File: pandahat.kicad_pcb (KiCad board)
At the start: 2 copper layers, 92 x 56 mm, 107 parts, among them CN1 Wago connector, CN2 Wago connector, CN3 Wago connector, CN4 Wago connector, CN5 Wago connector, CN6 Wago connector, CN7 Wago connector, J1 GPIO, J19 Conn_01x03, J2 Conn_02x03_Odd_Even, J20 Conn_01x03, J21 Conn_01x03, J3 Conn_01x04, SW1 TS-1187A-B-A-B, U1 AMS1117-3.3, U2 LM2596-5.0FW05ARHQ, U3 STM32F103C8T6, U6 LIS2DH12TR

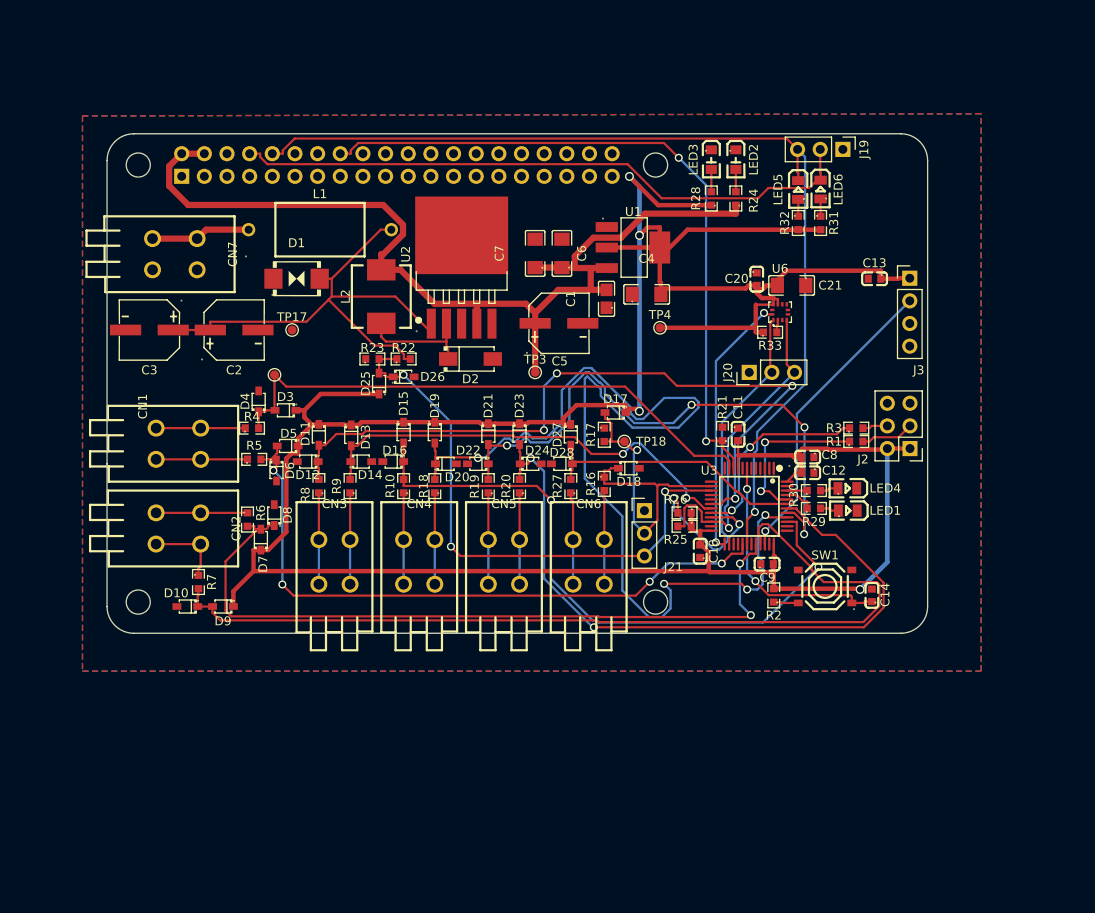
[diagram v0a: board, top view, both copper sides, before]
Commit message: changed IMU, reworked PCB layout
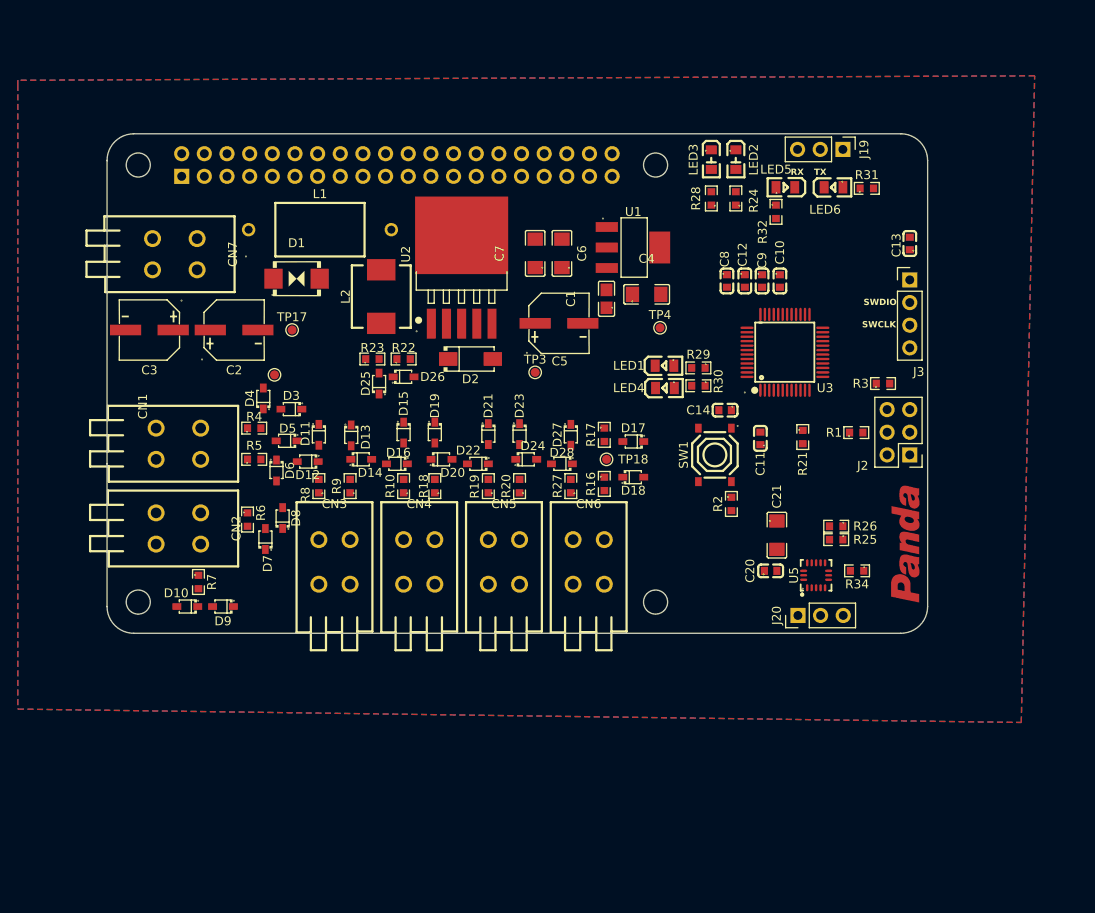
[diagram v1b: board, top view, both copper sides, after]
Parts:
- removed J21: Conn_01x03, Connector_PinHeader_2.54mm:PinHeader_1x03_P2.54mm_Vertical
- removed R33: 0603WAF1003T5E, easyeda2kicad:R0603
- removed U6: LIS2DH12TR, easyeda2kicad:LGA-12_L2.0-W2.0-P0.50-BL
- added G***: LOGO, LOGO, F.Cu at (189.5, 90.0)
- added R34: 0603WAF1003T5E, easyeda2kicad:R0603, F.Cu at (184.1, 93.0)
- added U5: LIS3DHTR_C15134, easyeda2kicad:LGA-16_L3.0-W3.0-P0.50-TL, F.Cu at (179.5, 93.5)
- moved C20 32.7 mm to (174.4, 93.0), turned to 0 degrees
- moved C9 31.8 mm to (173.4, 60.5), turned to -90 degrees
- moved C10 31.6 mm to (175.4, 60.5), turned to -90 degrees
- moved C21 28.0 mm to (175.1, 89.0), turned to -90 degrees
- moved J20 27.8 mm to (177.5, 98.0)
- moved C14 26.5 mm to (169.3, 75.0), turned to 180 degrees
- moved LED1 26.2 mm to (162.5, 70.0), turned to 0 degrees
- moved LED4 23.3 mm to (162.6, 72.5), turned to 0 degrees
- moved C12 22.6 mm to (171.5, 60.5), turned to -90 degrees
- moved C8 21.7 mm to (169.5, 60.5), turned to -90 degrees
- moved R29 20.4 mm to (166.3, 70.2), turned to 180 degrees
- moved SW1 19.2 mm to (168.2, 80.0), turned to -90 degrees
- moved U3 17.7 mm to (176.0, 68.5), turned to 0 degrees
- moved R30 17.5 mm to (166.3, 72.2), turned to 180 degrees
- moved R25 17.1 mm to (181.8, 89.5)
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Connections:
- J3 pad 3: /MCU_IO/STM32/SWDCLK -> /MCU_IO/STM32/SWCLK
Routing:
- net +3.3V: track 329.9 -> 0.00 mm, vias 4 -> 0
- net /MCU_IO/INPUT7: track 119.9 -> 0.00 mm, vias 4 -> 0
- net /UART_RX: track 111.2 -> 0.00 mm, vias 1 -> 0
- net +5V: track 110.9 -> 0.00 mm
- net /MCU_IO/INPUT3: track 101.3 -> 0.00 mm
- net /MCU_IO/INPUT2: track 83.1 -> 0.00 mm, vias 2 -> 0
- net /MCU_IO/INPUT4: track 82.0 -> 0.00 mm, vias 4 -> 0
- net /MCU_IO/INPUT9: track 78.1 -> 0.00 mm, vias 2 -> 0
- net /GPIO23: track 77.9 -> 0.00 mm, vias 2 -> 0
- net /MCU_IO/INPUT1: track 73.3 -> 0.00 mm, vias 4 -> 0
- net /MCU_IO/INPUT6: track 72.6 -> 0.00 mm, vias 2 -> 0
- net /UART_TX: track 70.8 -> 0.00 mm
- net /MCU_IO/INPUT8: track 65.7 -> 0.00 mm, vias 4 -> 0
- net /MCU_IO/ANALOG1: track 63.9 -> 0.00 mm, vias 3 -> 0
- net /MCU_IO/INPUT0: track 63.5 -> 0.00 mm
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- added copper zone on In1.Cu, net GND
- added copper zone on In2.Cu, net GND
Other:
- copper layers 2 -> 4
- board text added: "RX"
- board text added: "SWCLK"
- board text added: "SWDIO"
- board text added: "TX"

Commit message: manual routing progress
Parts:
- moved C11 17.2 mm to (181.2, 62.8), turned to 180 degrees
- moved C8 16.7 mm to (177.2, 75.2), turned to 90 degrees
- moved R34 14.8 mm to (180.2, 78.8), turned to -90 degrees
- moved C20 14.3 mm to (173.2, 78.8), turned to -90 degrees
- moved L2 13.9 mm to (141.8, 70.8), turned to 0 degrees
- moved U5 13.7 mm to (177.2, 80.0)
- moved C6 13.4 mm to (149.5, 70.8), turned to 0 degrees
- moved C14 12.0 mm to (168.9, 87.0)
- moved SW1 12.0 mm to (167.8, 92.0)
- moved C12 11.2 mm to (168.2, 71.2), turned to 0 degrees
- moved C3 11.2 mm to (115.8, 68.0)
- moved TP3 10.6 mm to (153.2, 61.5)
- moved C7 10.4 mm to (149.5, 67.8), turned to 0 degrees
- moved R2 9.71 mm to (172.0, 95.0), turned to 0 degrees
- moved TP4 9.34 mm to (164.5, 56.8)
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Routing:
- net +3.3V: track 0.00 -> 222.2 mm
- net +5V: track 0.00 -> 115.1 mm, vias 0 -> 5
- net VPP: track 0.00 -> 35.8 mm
- net /MCU_IO/STM32/RESET: track 0.00 -> 19.7 mm, vias 0 -> 2
- net /MCU_IO/PB11_SDA: track 0.00 -> 19.4 mm, vias 0 -> 1
- net /MCU_IO/STM32/BOOT0: track 0.00 -> 19.1 mm, vias 0 -> 2
- net /MCU_IO/PB10_SCL: track 0.00 -> 17.7 mm, vias 0 -> 1
- net +BATT: track 0.00 -> 11.2 mm
- net /MCU_IO/Analog Input/ANALOG_IN: track 0.00 -> 10.5 mm
- net /MCU_IO/INPUT9/INPUT: track 0.00 -> 10.2 mm
- net /MCU_IO/INPUT8/INPUT: track 0.00 -> 10.2 mm
- net /MCU_IO/INPUT7/INPUT: track 0.00 -> 10.2 mm
- net /MCU_IO/INPUT6/INPUT: track 0.00 -> 10.2 mm
- net /MCU_IO/INPUT5/INPUT: track 0.00 -> 10.2 mm
- net /MCU_IO/INPUT4/INPUT: track 0.00 -> 10.2 mm
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- added copper zone on F.Cu, net +3.3V
- removed copper zone on In1.Cu, net GND
- removed copper zone on In2.Cu, net GND
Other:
- copper layers 4 -> 2

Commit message: more work
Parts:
- added D29: SS54_C22452, easyeda2kicad:SMA_L4.4-W2.8-LS5.4-R-RD, F.Cu at (119.7, 66.3)
- L2: value FXL0630-6R8-M -> 47uH; footprint easyeda2kicad:IND-SMD_L7.0-W6.6 -> easyeda2kicad:IND-SMD_L7.2-W6.6_GPSR07X0
- moved TP17 40.9 mm to (160.2, 87.8)
- moved J19 37.7 mm to (145.4, 52.5), turned to 90 degrees
- moved R31 37.2 mm to (149.1, 59.1), turned to -90 degrees
- moved J2 33.0 mm to (168.8, 51.8)
- moved C10 32.8 mm to (148.5, 62.0), turned to 0 degrees
- moved LED6 32.5 mm to (149.5, 56.0), turned to -90 degrees
- moved R1 31.2 mm to (163.9, 52.0), turned to 90 degrees
- moved LED2 31.1 mm to (140.7, 56.0)
- moved SW1 30.5 mm to (171.8, 61.8)
- moved R24 30.5 mm to (141.0, 59.1)
- moved C14 30.3 mm to (169.9, 56.7), turned to 90 degrees
- moved R3 30.0 mm to (162.4, 52.2), turned to 90 degrees
- moved LED5 29.2 mm to (147.5, 56.0), turned to -90 degrees
- moved R2 28.2 mm to (169.9, 66.9), turned to -90 degrees
- moved R32 28.1 mm to (147.6, 59.1)
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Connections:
- C2 pad 1: VPP -> Net-(D29-K)
- C3 pad 1: VPP -> Net-(D29-K)
- D1 pad 2: VPP -> +BATT
- J19 pad 2: /UART_TX -> /UART_RX
- J19 pad 3: /UART_RX -> /UART_TX
- J3 pad 1: +3.3V -> GND
- J3 pad 2: /MCU_IO/STM32/SWDIO -> /MCU_IO/STM32/SWCLK
- J3 pad 3: /MCU_IO/STM32/SWCLK -> /MCU_IO/STM32/SWDIO
- J3 pad 4: GND -> +3.3V
- R2 pad 1: Net-(SW1-B) -> Net-(SW1-D)
- SW1 pad 1: /MCU_IO/STM32/RESET -> GND
- SW1 pad 2: Net-(SW1-B) -> unconnected-(SW1-B-Pad2)
- SW1 pad 3: GND -> /MCU_IO/STM32/RESET
- SW1 pad 4: unconnected-(SW1-D-Pad4) -> Net-(SW1-D)
- U2 pad 1: VPP -> Net-(D29-K)
- U3 pad 31: /MCU_IO/STM32/STMRX -> /UART_TX
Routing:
- net /MCU_IO/INPUT3: track 3.69 -> 83.9 mm, vias 0 -> 2
- net /MCU_IO/INPUT2: track 4.05 -> 68.0 mm, vias 0 -> 2
- net /MCU_IO/INPUT1: track 3.96 -> 61.1 mm, vias 0 -> 2
- net /MCU_IO/INPUT0: track 6.38 -> 61.8 mm, vias 0 -> 4
- net +3.3V: track 222.2 -> 167.2 mm
- net /MCU_IO/INPUT4: track 3.90 -> 58.5 mm, vias 0 -> 2
- net /MCU_IO/INPUT5: track 3.82 -> 52.8 mm, vias 0 -> 2
- net /UART_TX: track 4.43 -> 50.2 mm, vias 0 -> 1
- net /GPIO23: track 0.00 -> 44.3 mm, vias 0 -> 2
- net +5V: track 115.1 -> 73.2 mm, vias 5 -> 2
- net /UART_RX: track 4.38 -> 44.1 mm, vias 0 -> 1
- net /MCU_IO/STM32/SWCLK: track 0.00 -> 37.6 mm, vias 0 -> 1
- net /MCU_IO/STM32/SWDIO: track 0.00 -> 32.4 mm, vias 0 -> 1
- net /MCU_IO/INPUT6: track 4.43 -> 36.5 mm, vias 0 -> 2
- net /MCU_IO/ANALOG0: track 8.37 -> 40.3 mm, vias 0 -> 4
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- added copper zone on F.Cu, net +5V
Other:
- board size 92 x 56 mm -> 88 x 56 mm
- board text removed: "DISPLAY (OPTIONAL)"
- board text removed: "RX"
- board text removed: "SWCLK"
- board text removed: "SWDIO"
- board text removed: "TX"

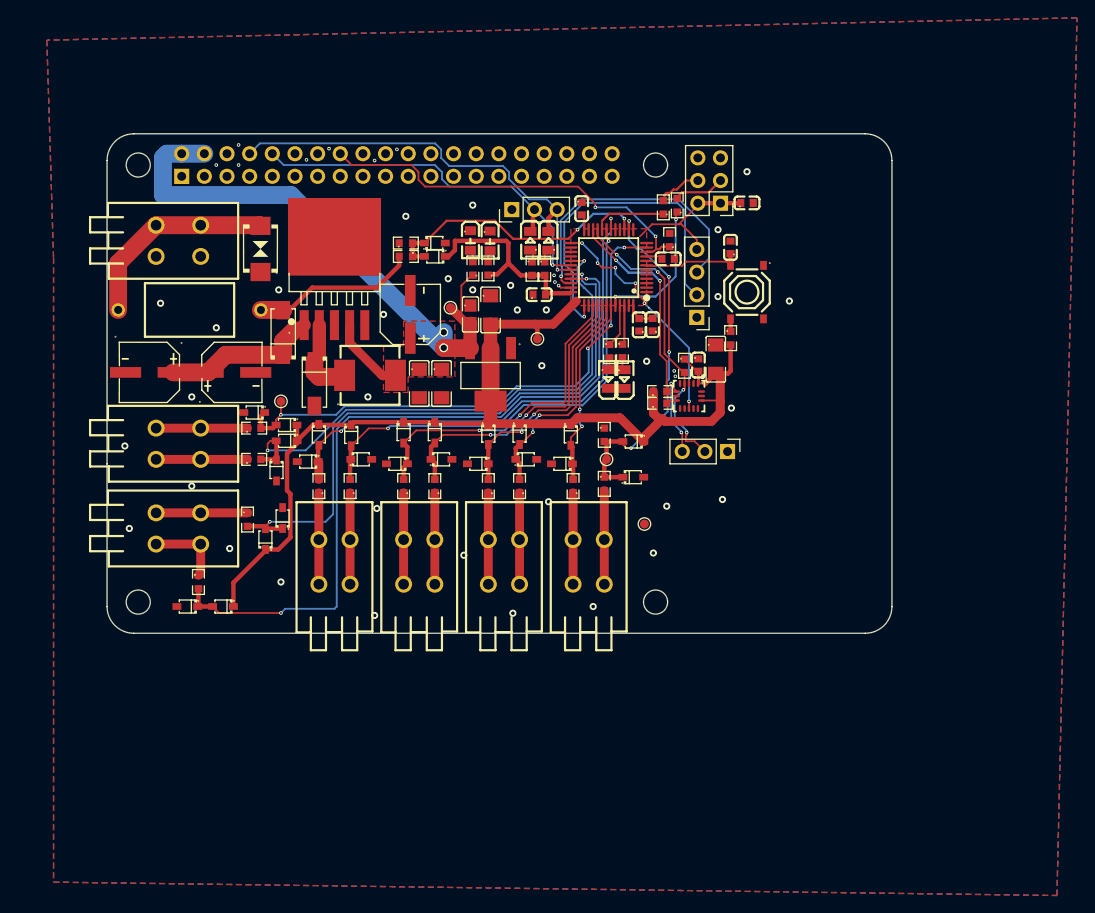
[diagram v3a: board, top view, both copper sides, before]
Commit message: fully routed
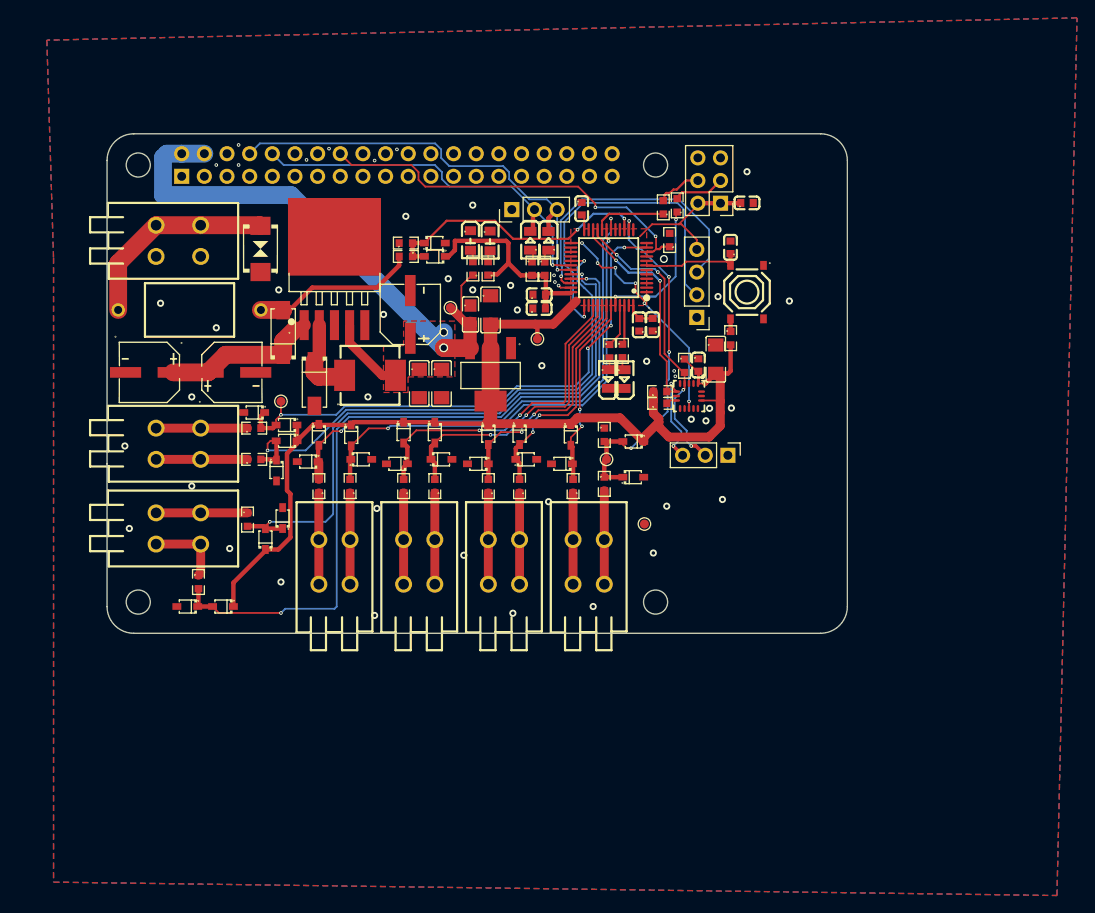
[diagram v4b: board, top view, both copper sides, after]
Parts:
- added G***: LOGO, LOGO, F.Cu at (178.0, 53.5)
- moved G*** 21.1 mm to (174.0, 93.5), turned to 0 degrees
- moved C12 15.5 mm to (148.4, 63.6), turned to 0 degrees
- moved J20 0.42 mm to (169.6, 80.0)
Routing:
- net +3.3V: track 167.2 -> 169.8 mm
- net /MCU_IO/PB11_SDA: track 33.6 -> 34.7 mm
- net GND: vias 46 -> 49
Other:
- board size 88 x 56 mm -> 83 x 56 mm
- board text added: "@stack_smash"

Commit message: Finished pcb
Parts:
- added CN13: B2B-PH-K-S, easyeda2kicad:CONN-TH_B2B-PH-K-S, F.Cu at (181.1, 56.0)
- added CN14: B2B-PH-K-S, easyeda2kicad:CONN-TH_B2B-PH-K-S, F.Cu at (176.3, 56.0)
- added CN15: B2B-PH-K-S, easyeda2kicad:CONN-TH_B2B-PH-K-S, F.Cu at (181.1, 49.8)
- added CN16: B2B-PH-K-S, easyeda2kicad:CONN-TH_B2B-PH-K-S, F.Cu at (176.3, 49.8)
- added CN8: JST 4PIN, easyeda2kicad:CONN-TH_B4B-PH-K-S, F.Cu at (169.3, 87.5)
- added R35: 0603WAF1002T5E, easyeda2kicad:R0603, F.Cu at (164.8, 86.5)
- added R36: 0603WAF1002T5E, easyeda2kicad:R0603, F.Cu at (164.8, 88.5)
- moved LED1 18.6 mm to (146.5, 55.6), turned to 0 degrees
- moved G*** 18.5 mm to (177.7, 72.0)
- moved LED4 18.2 mm to (146.5, 57.4), turned to 0 degrees
- moved R31 15.4 mm to (134.5, 54.2), turned to 0 degrees
- moved LED6 15.2 mm to (134.8, 52.2), turned to 180 degrees
- moved R29 14.5 mm to (149.8, 55.5), turned to 180 degrees
- moved R30 13.7 mm to (149.7, 57.2), turned to 180 degrees
- moved LED5 8.79 mm to (139.5, 52.2), turned to 0 degrees
- moved R32 8.76 mm to (142.4, 52.1)
- moved G*** 2.15 mm to (173.5, 95.6)
- moved R25 1.35 mm to (161.0, 72.0), turned to 90 degrees
- moved J19 0.52 mm to (145.2, 52.0)
- moved C8 0.06 mm to (161.2, 65.4)
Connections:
- net /MCU_IO/PB10_SCL renamed /MCU_IO/IMU_SCL
- net /MCU_IO/PB11_SDA renamed /MCU_IO/IMU_SDA
- U3 pad 2: unconnected-(U3-PC13-TAMPER-RTC-Pad2) -> /MCU_IO/Gpio expose5/PIN
- U3 pad 26: /MCU_IO/STM32/PB13 -> /MCU_IO/LED1
- U3 pad 27: /MCU_IO/STM32/PB14 -> /MCU_IO/LED2
- U3 pad 3: unconnected-(U3-PC14-OSC32_IN-Pad3) -> /MCU_IO/Gpio expose6/PIN
- U3 pad 4: unconnected-(U3-PC15-OSC32_OUT-Pad4) -> /MCU_IO/Gpio expose7/PIN
- U3 pad 45: /MCU_IO/LED1 -> /MCU_IO/EXTRA_SCL
- U3 pad 46: /MCU_IO/LED2 -> /MCU_IO/EXTRA_SDA
- U3 pad 5: unconnected-(U3-PD0-OSC_IN-Pad5) -> /MCU_IO/Gpio expose8/PIN
- U3 pad 6: unconnected-(U3-PD1-OSC_OUT-Pad6) -> /MCU_IO/STM32/PD1
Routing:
- net +3.3V: track 169.8 -> 204.6 mm, vias 0 -> 2
- net /MCU_IO/EXTRA_SCL: track 0.00 -> 34.7 mm, vias 0 -> 2
- net /MCU_IO/EXTRA_SDA: track 0.00 -> 33.0 mm, vias 0 -> 2
- net /MCU_IO/Gpio expose5/PIN: track 0.00 -> 28.6 mm, vias 0 -> 1
- net /MCU_IO/Gpio expose7/PIN: track 0.00 -> 27.8 mm, vias 0 -> 1
- net /MCU_IO/Gpio expose6/PIN: track 0.00 -> 24.8 mm, vias 0 -> 1
- net /MCU_IO/Gpio expose8/PIN: track 0.00 -> 22.4 mm, vias 0 -> 1
- net GND: track 1.47 -> 5.22 mm, vias 49 -> 77
- net /UART_TX: track 50.2 -> 53.7 mm, vias 1 -> 2
- net /MCU_IO/IMU_SCL: track 33.0 -> 36.3 mm
- net /MCU_IO/LED2: track 4.44 -> 1.54 mm
- net /MCU_IO/ANALOG0: track 40.3 -> 42.9 mm
- net /MCU_IO/LED1: track 4.85 -> 2.30 mm
- net /MCU_IO/IMU_SDA: track 34.7 -> 37.2 mm
- net /MCU_IO/STM32/BOOT0: track 16.0 -> 18.4 mm
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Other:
- board text added: "+12V !!!!!"
- board text added: "1"
- board text added: "10"
- board text added: "11"
- board text added: "2"
- board text added: "3"
- board text added: "3.3V"
- board text added: "4"
- board text added: "5"
- board text added: "6"
- board text added: "7"
- board text added: "8"
- board text added: "9"
- board text added: "A1"
- board text added: "Debug here ------>"
- board text added: "Flip the board, wrong side"
- board text added: "GND"
- board text added: "I hope this doesn't blow up ----->"
- board text added: "If these light up it's working(?)"
- board text added: "If you can read this something went really wrong"
- board text added: "PC13"
- board text added: "PC14"
- board text added: "PC15"
- board text added: "PD0"
- board text added: "RST"
- board text added: "RX"
- board text added: "SCL"
- board text added: "SDA"
- board text added: "SWCLK"
- board text added: "SWDIO"
- board text added: "TX"
- board text added: "This thing senses shit <----"
- board text added: "This too can blow up <----"
- board text added: "VCC"
- board text added: "cheapest stm32 money can buy <-------"
- board text added: "t.me/stack_log"
- board text added: "x | y-(z)"
